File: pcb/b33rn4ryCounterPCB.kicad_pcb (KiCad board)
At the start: 2 copper layers, 65 x 56 mm, 14 parts, among them J1 RPi_GPIO, P1 Display 20x4, P2 Counter, P3 Console, P4 12V, P5 RTC, Q1 BC548, Q2 IRL2203N

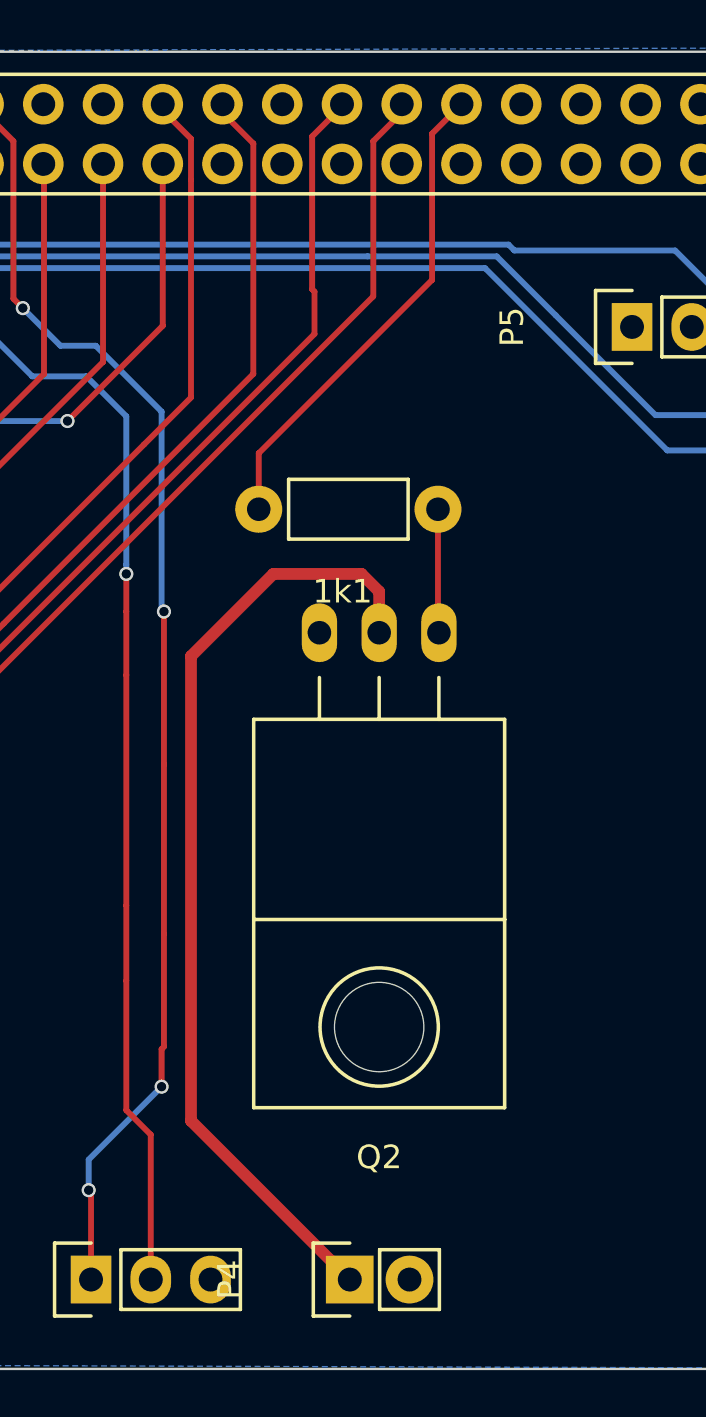
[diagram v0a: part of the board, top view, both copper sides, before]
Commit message: Add 1N5000 diode
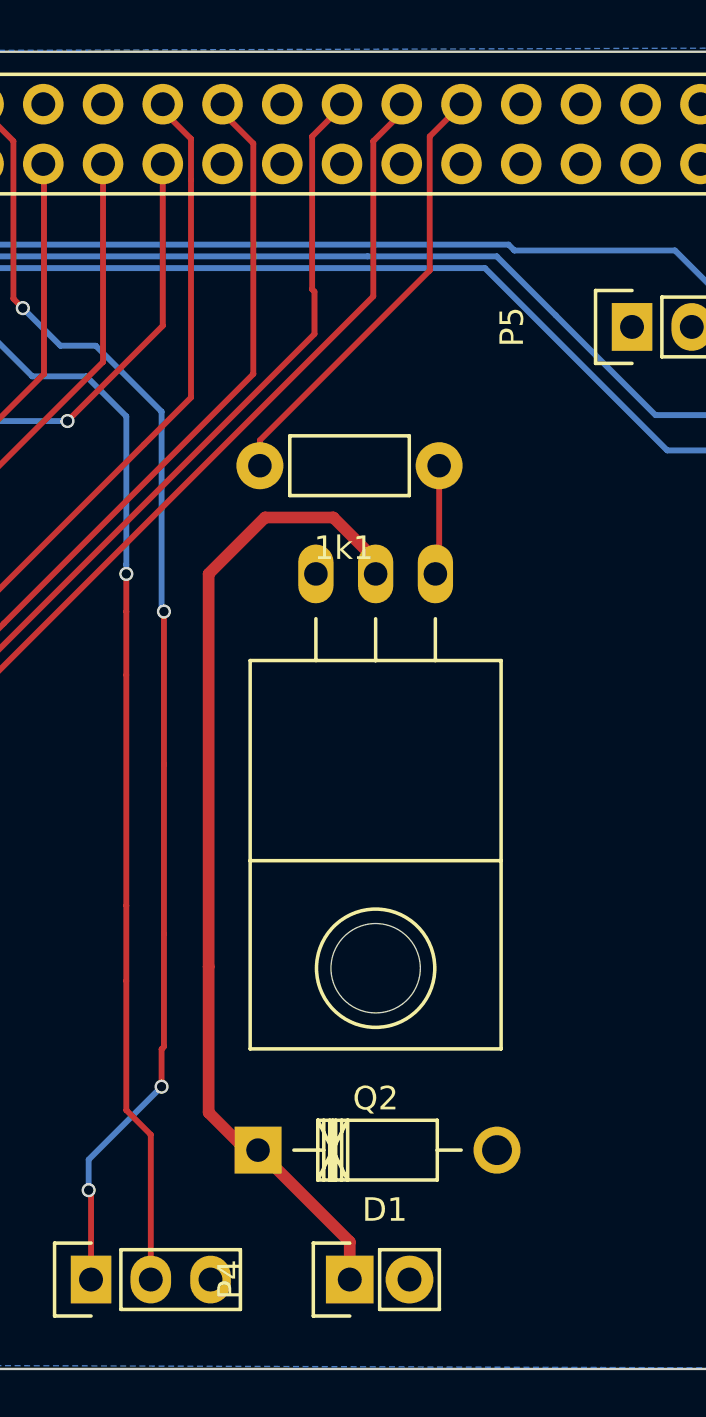
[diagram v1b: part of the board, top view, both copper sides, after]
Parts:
- added D1: 1N5000, Diodes_ThroughHole:Diode_DO-41_SOD81_Horizontal_RM10, F.Cu at (78.6, 97.5)
- P4: value 12V -> Switch
- moved Q2 2.50 mm to (83.6, 73.0)
- moved 1k1 1.85 mm to (86.3, 68.4)
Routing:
- net Net-(1k1-Pad2): track 20.8 -> 18.9 mm
- net Net-(D1-Pad1): track 40.8 -> 42.3 mm
- net Net-(1k1-Pad1): track 5.27 -> 4.67 mm
